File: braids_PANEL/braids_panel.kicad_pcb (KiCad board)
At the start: 2 copper layers, 100 x 200 mm, 23 parts

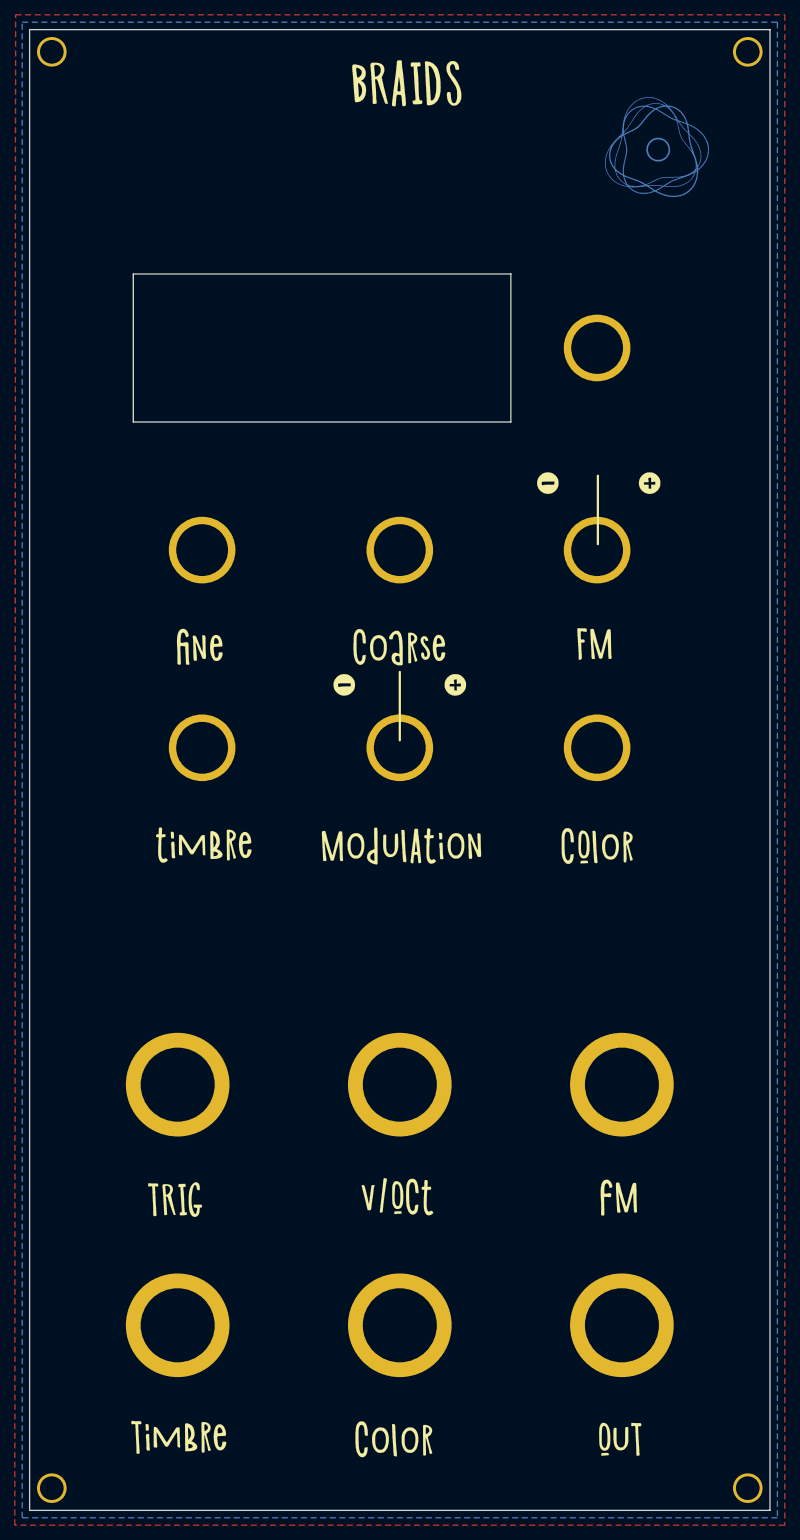
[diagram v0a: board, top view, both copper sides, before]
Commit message: add trim switch
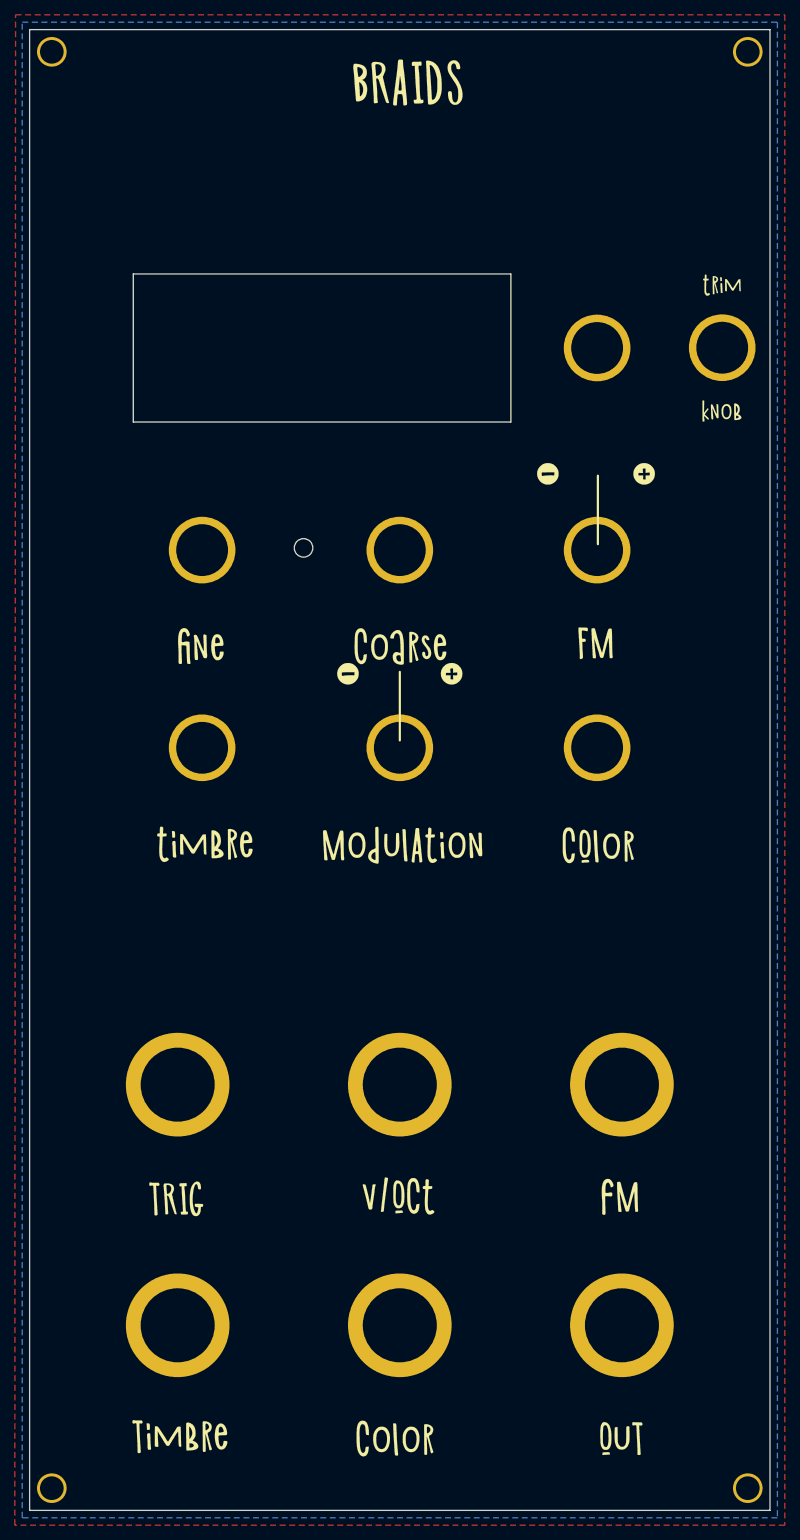
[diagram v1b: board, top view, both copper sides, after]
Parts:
- removed the G*** at (157.5, 138.5)
- removed the G*** at (142.5, 138.5)
- removed the G*** at (183.8, 111.2)
- removed the G*** at (170.0, 111.2)
- removed the G*** at (184.7, 65.9)
- added  : tuneswitch, Kosmo_panel:Kosmo_Switch_Hole, F.Cu at (193.5, 93.0)
- added G***: LOGO, braids_panel:braids_knob, F.Cu at (193.5, 101.5)
- added G***: LOGO, braids_panel:braids_trim, F.Cu at (193.5, 84.5)
- added G***: LOGO, braids_panel:braids_plus_symbol, F.Cu at (157.0, 137.0)
- added G***: LOGO, braids_panel:braids_minus_symbol, F.Cu at (143.0, 137.0)
- added G***: LOGO, braids_panel:braids_plus_symbol, F.Cu at (183.0, 110.0)
- added G***: LOGO, braids_panel:braids_minus_symbol, F.Cu at (170.0, 110.0)
- added H12: minitune, Kosmo_panel:Kosmo_Trimmer_Pot_Hole, F.Cu at (137.0, 120.0)
- moved G*** 0.18 mm to (150.0, 150.0)
